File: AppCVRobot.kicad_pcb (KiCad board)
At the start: 2 copper layers, 17 parts, among them U2 IZOKEEProMini

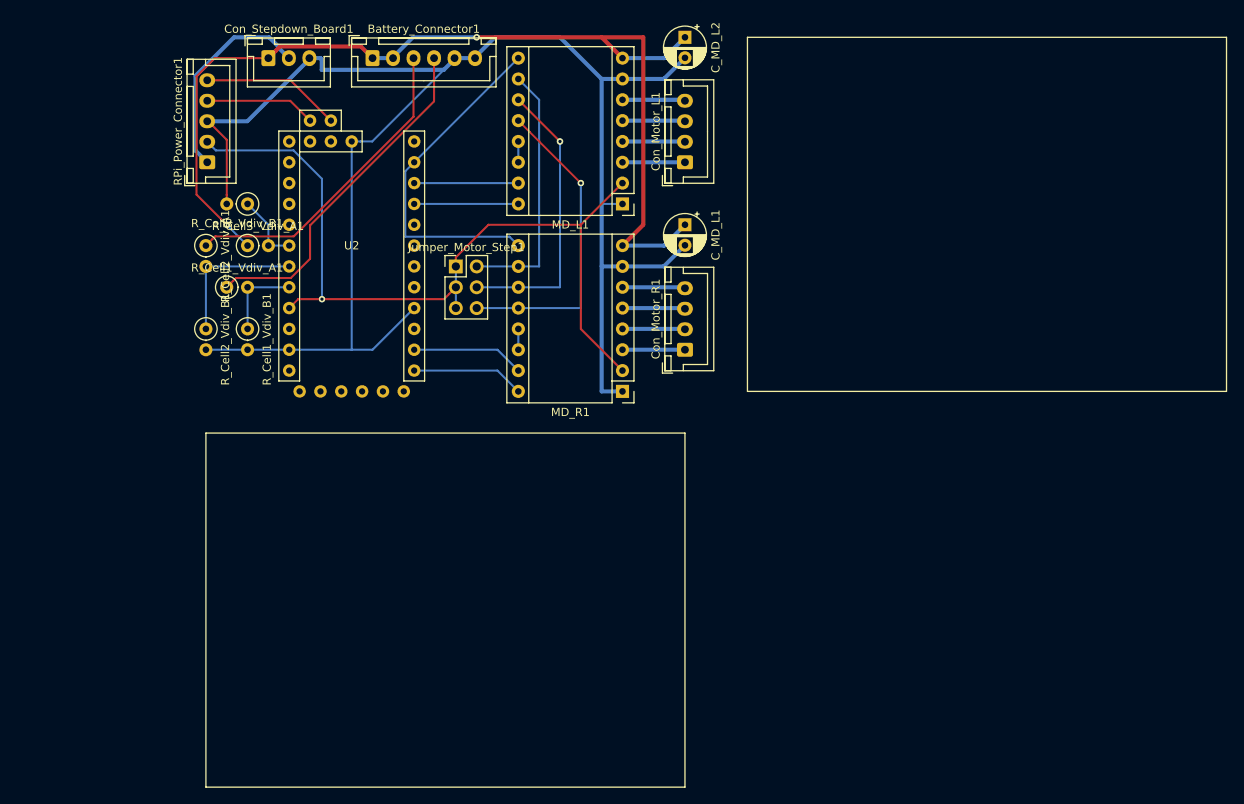
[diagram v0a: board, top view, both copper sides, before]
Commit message: Board split into main and power. Proper voltage difference forming to get cell voltages. current measurement.
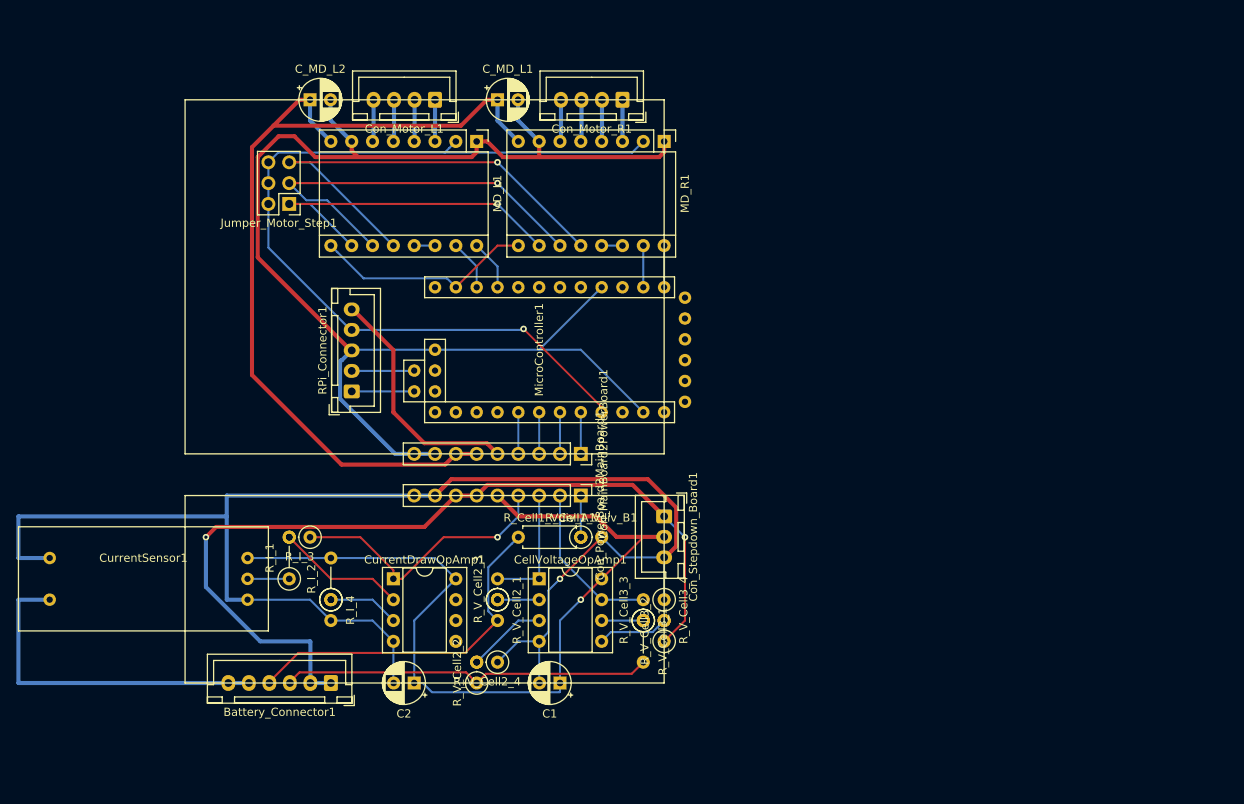
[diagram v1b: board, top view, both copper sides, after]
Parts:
- removed RPi_Power_Connector1: Conn_01x05, Connector_JST:JST_XH_B5B-XH-A_1x05_P2.50mm_Vertical
- removed R_Cell2_Vdiv_A1, R_Cell3_Vdiv_A1: 100K, Resistor_THT:R_Axial_DIN0207_L6.3mm_D2.5mm_P2.54mm_Vertical
- removed R_Cell2_Vdiv_B1: 47K, Resistor_THT:R_Axial_DIN0207_L6.3mm_D2.5mm_P2.54mm_Vertical
- removed R_Cell3_Vdiv_B1: 33K, Resistor_THT:R_Axial_DIN0207_L6.3mm_D2.5mm_P2.54mm_Vertical
- removed U2: IZOKEEProMini, CustomFootprints:Arduino_Pro_Mini_Socket_IZOKEE
- added C1: 1uF, Capacitor_THT:CP_Radial_D5.0mm_P2.50mm, F.Cu at (175.3, 101.6)
- added C2: 1uF, Capacitor_THT:CP_Radial_D5.0mm_P2.50mm, F.Cu at (157.5, 101.6)
- added CellVoltageOpAmp1: LM358, Package_DIP:DIP-8_W7.62mm_Socket, F.Cu at (172.7, 88.9)
- added Con_MainBoard2PowerBoard1: Conn_01x09_Female, Connector_PinSocket_2.54mm:PinSocket_1x09_P2.54mm_Vertical, F.Cu at (177.8, 73.7)
- added Con_PowerBoard2MainBoard1: Conn_01x09_Male, Connector_PinHeader_2.54mm:PinHeader_1x09_P2.54mm_Vertical, F.Cu at (177.8, 78.7)
- added CurrentDrawOpAmp1: LM358, Package_DIP:DIP-8_W7.62mm_Socket, F.Cu at (154.9, 88.9)
- added CurrentSensor1: ACS712Breakout, CustomFootprints:ACS712BreakoutBoardUpSideDown, F.Cu at (124.5, 88.9)
- added MicroController1: IZOKEEProMini, CustomFootprints:Arduino_Pro_Mini_Socket_IZOKEE, F.Cu at (175.3, 61.0)
- added RPi_Connector1: Conn_01x05, Connector_JST:JST_XH_B5B-XH-A_1x05_P2.50mm_Vertical, F.Cu at (149.9, 66.0)
- added R_I_1: 10K, Resistor_THT:R_Axial_DIN0207_L6.3mm_D2.5mm_P5.08mm_Vertical, F.Cu at (142.2, 88.9)
- added R_I_2: 33K, Resistor_THT:R_Axial_DIN0207_L6.3mm_D2.5mm_P5.08mm_Vertical, F.Cu at (147.3, 91.4)
- added R_I_3: 33K, Resistor_THT:R_Axial_DIN0207_L6.3mm_D2.5mm_P2.54mm_Vertical, F.Cu at (144.8, 83.8)
- added R_I_4: 22K, Resistor_THT:R_Axial_DIN0207_L6.3mm_D2.5mm_P2.54mm_Vertical, F.Cu at (147.3, 91.4)
- added R_V_Cell2_1: 47K, Resistor_THT:R_Axial_DIN0207_L6.3mm_D2.5mm_P2.54mm_Vertical, F.Cu at (167.6, 91.4)
- added R_V_Cell2_2: 47K, Resistor_THT:R_Axial_DIN0207_L6.3mm_D2.5mm_P2.54mm_Vertical, F.Cu at (165.1, 101.6)
- added R_V_Cell2_3: 33K, Resistor_THT:R_Axial_DIN0207_L6.3mm_D2.5mm_P2.54mm_Vertical, F.Cu at (167.6, 91.4)
- added R_V_Cell2_4: 33K, Resistor_THT:R_Axial_DIN0207_L6.3mm_D2.5mm_P2.54mm_Vertical, F.Cu at (167.6, 99.1)
- added R_V_Cell3_1: 47K, Resistor_THT:R_Axial_DIN0207_L6.3mm_D2.5mm_P5.08mm_Vertical, F.Cu at (185.4, 94.0)
- added R_V_Cell3_2: 47K, Resistor_THT:R_Axial_DIN0207_L6.3mm_D2.5mm_P2.54mm_Vertical, F.Cu at (188.0, 96.5)
- added R_V_Cell3_3: 33K, Resistor_THT:R_Axial_DIN0207_L6.3mm_D2.5mm_P2.54mm_Vertical, F.Cu at (185.4, 94.0)
- added R_V_Cell3_4: 33K, Resistor_THT:R_Axial_DIN0207_L6.3mm_D2.5mm_P2.54mm_Vertical, F.Cu at (188.0, 91.4)
- R_Cell1_Vdiv_A1: footprint Resistor_THT:R_Axial_DIN0207_L6.3mm_D2.5mm_P2.54mm_Vertical -> Resistor_THT:R_Axial_DIN0207_L6.3mm_D2.5mm_P7.62mm_Horizontal
- moved Battery_Connector1 76.4 mm to (147.3, 101.6), turned to 180 degrees
- moved Con_Stepdown_Board1 73.8 mm to (188.0, 81.3), turned to 270 degrees
- moved R_Cell1_Vdiv_B1 47.9 mm to (177.8, 83.8), turned to 0 degrees
- moved R_Cell1_Vdiv_A1 46.8 mm to (170.2, 83.8)
- moved C_MD_L2 46.4 mm to (144.8, 30.5), turned to 0 degrees
- moved Con_Motor_R1 31.4 mm to (182.9, 30.5), turned to 180 degrees
- moved Con_Motor_L1 31.4 mm to (160.0, 30.5), turned to 180 degrees
- moved MD_R1 30.9 mm to (188.0, 35.6), turned to 270 degrees
- moved C_MD_L1 27.5 mm to (167.6, 30.5), turned to 0 degrees
- moved Jumper_Motor_Step1 21.7 mm to (142.2, 43.2), turned to 180 degrees
- moved MD_L1 19.3 mm to (165.1, 35.6), turned to 270 degrees
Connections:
- Battery_Connector1 pad 5: GND -> Net-(Battery_Connector1-Pad5)
- Battery_Connector1 pad 6: GND -> Net-(Battery_Connector1-Pad5)
- Jumper_Motor_Step1 pad 1: +3V3 -> MS1
- Jumper_Motor_Step1 pad 2: MS1 -> +3V3
- Jumper_Motor_Step1 pad 3: +3V3 -> MS2
- Jumper_Motor_Step1 pad 4: MS2 -> +3V3
- Jumper_Motor_Step1 pad 5: +3V3 -> MS3
- Jumper_Motor_Step1 pad 6: MS3 -> +3V3
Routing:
- net +5V: track 25.6 -> 137.1 mm, vias 0 -> 1
- net GND: track 247.0 -> 351.9 mm, vias 0 -> 1
- net +BATT: track 156.3 -> 217.2 mm
- net Net-(Battery_Connector1-Pad5): track 0.00 -> 42.1 mm
- net Net-(Con_PowerBoard2MainBoard1-Pad4): track 0.00 -> 33.8 mm, vias 0 -> 1
- net Net-(CellVoltageOpAmp1-Pad7): track 0.00 -> 19.9 mm
- net MS3: track 38.7 -> 56.7 mm
- net Net-(R_Cell2_Vdiv_A1-Pad2): track 17.8 -> 0.00 mm
- net Net-(CurrentDrawOpAmp1-Pad2): track 0.00 -> 15.9 mm
- net Net-(CellVoltageOpAmp1-Pad1): track 0.00 -> 15.2 mm
- net Enable_Steppers: track 41.7 -> 27.1 mm
- net MS2: track 35.1 -> 49.5 mm
- net MS1: track 31.5 -> 42.3 mm, vias 0 -> 1
- net Net-(CellVoltageOpAmp1-Pad3): track 0.00 -> 9.72 mm
- net I2C_SCL: track 17.1 -> 7.64 mm
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
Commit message: Added levelshifter for LCD display
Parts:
- added Display_Connector1: Conn_01x04, Connector_JST:JST_XH_B4B-XH-A_1x04_P2.50mm_Vertical, F.Cu at (132.1, 49.4)
- added U1: LevelShifter, CustomFootprints:LevelShifterBreakoutBoard, F.Cu at (135.9, 59.7)
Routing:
- net GND: track 351.9 -> 386.2 mm, vias 1 -> 2
- net +5V: track 137.1 -> 168.7 mm
- net Net-(Display_Connector1-Pad4): track 0.00 -> 27.3 mm
- net Net-(Display_Connector1-Pad3): track 0.00 -> 21.9 mm
- net +3V3: track 108.5 -> 119.1 mm
- net I2C_SCL: track 7.64 -> 17.7 mm
- net I2C_SDA: track 7.62 -> 17.0 mm
- net +BATT: track 217.2 -> 213.5 mm

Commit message: Various fixes/mods while building
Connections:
- Battery_Connector1 pad 1: +BATT -> BATT_Cell_2_3
- Battery_Connector1 pad 2: +BATT -> BATT_Cell_1_2
- Battery_Connector1 pad 3: BATT_Cell_2_3 -> +BATT
- Battery_Connector1 pad 4: BATT_Cell_1_2 -> +BATT
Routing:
- net +BATT: track 213.5 -> 208.1 mm
- net BATT_Cell_2_3: track 45.3 -> 40.2 mm
- net BATT_Cell_1_2: track 43.2 -> 38.2 mm
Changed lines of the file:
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@@
     (thickness 1.6)
     (drawings 8)
-    (tracks 287)
+    (tracks 286)
     (zones 0)
     (modules 34)
@@
       (net 27 "Net-(Battery_Connector1-Pad5)"))
     (pad 4 thru_hole oval (at 7.5 0 180) (size 1.7 1.95) (drill 0.95) (layers *.Cu *.Mask)
+      (net 3 +BATT))
+    (pad 3 thru_hole oval (at 5 0 180) (size 1.7 1.95) (drill 0.95) (layers *.Cu *.Mask)
+      (net 3 +BATT))
+    (pad 2 thru_hole oval (at 2.5 0 180) (size 1.7 1.95) (drill 0.95) (layers *.Cu *.Mask)
       (net 15 BATT_Cell_1_2))
-    (pad 3 thru_hole oval (at 5 0 180) (size 1.7 1.95) (drill 0.95) (layers *.Cu *.Mask)
+    (pad 1 thru_hole roundrect (at 0 0 180) (size 1.7 1.95) (drill 0.95) (layers *.Cu *.Mask) (roundrect_rratio 0.147059)
       (net 16 BATT_Cell_2_3))
-    (pad 2 thru_hole oval (at 2.5 0 180) (size 1.7 1.95) (drill 0.95) (layers *.Cu *.Mask)
-      (net 3 +BATT))
-    (pad 1 thru_hole roundrect (at 0 0 180) (size 1.7 1.95) (drill 0.95) (layers *.Cu *.Mask) (roundrect_rratio 0.147059)
-      (net 3 +BATT))
     (model ${KISYS3DMOD}/Connector_JST.3dshapes/JST_XH_B6B-XH-A_1x06_P2.50mm_Vertical.wrl
       (at (xyz 0 0 0))
@@
   (segment (start 140.32 33.64) (end 143.48 30.48) (width 0.5) (layer F.Cu) (net 3))
   (segment (start 137.699989 36.260011) (end 140.32 33.64) (width 0.5) (layer F.Cu) (net 3))
-  (segment (start 144.82 101.6) (end 147.32 101.6) (width 0.5) (layer B.Cu) (net 3))
-  (segment (start 144.82 101.6) (end 144.82 96.56) (width 0.5) (layer B.Cu) (net 3))
-  (segment (start 144.82 96.56) (end 144.78 96.52) (width 0.5) (layer B.Cu) (net 3))
   (via (at 132.08 83.82) (size 0.8) (drill 0.4) (layers F.Cu B.Cu) (net 3))
-  (segment (start 132.08 89.889963) (end 132.08 83.82) (width 0.5) (layer B.Cu) (net 3))
-  (segment (start 144.78 96.52) (end 138.710037 96.52) (width 0.5) (layer B.Cu) (net 3))
-  (segment (start 138.710037 96.52) (end 132.08 89.889963) (width 0.5) (layer B.Cu) (net 3))
   (segment (start 132.08 83.82) (end 133.330001 82.569999) (width 0.5) (layer F.Cu) (net 3))
   (via (at 190.5 83.82) (size 0.8) (drill 0.4) (layers F.Cu B.Cu) (net 3))
@@
   (segment (start 163.685001 97.934999) (end 166.840001 94.779999) (width 0.25) (layer F.Cu) (net 15))
   (segment (start 166.840001 94.779999) (end 167.64 93.98) (width 0.25) (layer F.Cu) (net 15))
-  (segment (start 143.360001 97.934999) (end 163.685001 97.934999) (width 0.25) (layer F.Cu) (net 15))
-  (segment (start 139.82 101.475) (end 143.360001 97.934999) (width 0.25) (layer F.Cu) (net 15))
-  (segment (start 139.82 101.6) (end 139.82 101.475) (width 0.25) (layer F.Cu) (net 15))
-  (segment (start 143.49501 100.29999) (end 142.32 101.475) (width 0.25) (layer F.Cu) (net 16))
-  (segment (start 142.32 101.475) (end 142.32 101.6) (width 0.25) (layer F.Cu) (net 16))
-  (segment (start 163.79999 100.29999) (end 143.49501 100.29999) (width 0.25) (layer F.Cu) (net 16))
+  (segment (start 139.82 101.6) (end 139.82 101.475) (width 0.25) (layer F.Cu) (net 3))
+  (segment (start 142.32 101.475) (end 142.32 101.6) (width 0.25) (layer F.Cu) (net 3))
+  (segment (start 132.08 89.889963) (end 132.08 83.82) (width 0.5) (layer B.Cu) (net 3))
+  (segment (start 139.82 101.6) (end 139.82 97.629963) (width 0.5) (layer B.Cu) (net 3))
+  (segment (start 139.82 97.629963) (end 132.08 89.889963) (width 0.5) (layer B.Cu) (net 3))
+  (segment (start 142.32 101.6) (end 139.82 101.6) (width 0.5) (layer B.Cu) (net 3))
+  (segment (start 148.360001 97.934999) (end 163.685001 97.934999) (width 0.25) (layer F.Cu) (net 15))
+  (segment (start 144.82 101.475) (end 148.360001 97.934999) (width 0.25) (layer F.Cu) (net 15))
+  (segment (start 144.82 101.6) (end 144.82 101.475) (width 0.25) (layer F.Cu) (net 15))
   (segment (start 165.1 101.6) (end 163.79999 100.29999) (width 0.25) (layer F.Cu) (net 16))
   (segment (start 184.005001 100.474999) (end 185.42 99.06) (width 0.25) (layer F.Cu) (net 16))
   (segment (start 165.1 101.6) (end 166.225001 100.474999) (width 0.25) (layer F.Cu) (net 16))
   (segment (start 166.225001 100.474999) (end 184.005001 100.474999) (width 0.25) (layer F.Cu) (net 16))
+  (segment (start 148.62001 100.29999) (end 163.79999 100.29999) (width 0.25) (layer F.Cu) (net 16))
+  (segment (start 147.32 101.6) (end 148.62001 100.29999) (width 0.25) (layer F.Cu) (net 16))
   (segment (start 152.52 35.44) (end 152.4 35.56) (width 0.5) (layer B.Cu) (net 17))
   (segment (start 152.52 30.48) (end 152.52 35.44) (width 0.5) (layer B.Cu) (net 17))
